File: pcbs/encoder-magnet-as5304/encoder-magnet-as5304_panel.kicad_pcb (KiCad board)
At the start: 2 copper layers, 39 x 25 mm, 168 parts, among them J1 BM05B-GHS, Q1 BC807-40LWX, U1 AS5304

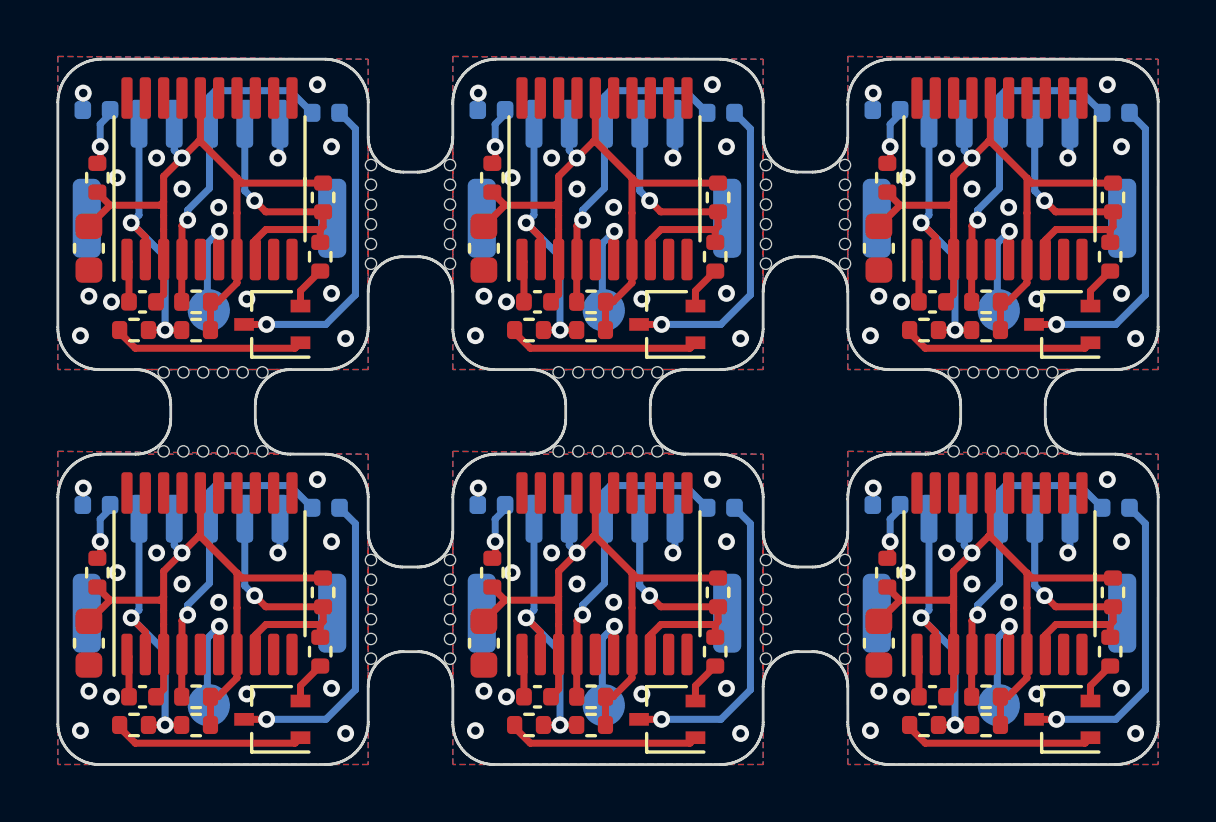
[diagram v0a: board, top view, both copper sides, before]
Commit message: Manually redraw broken outline for panelized AS5304 PCB
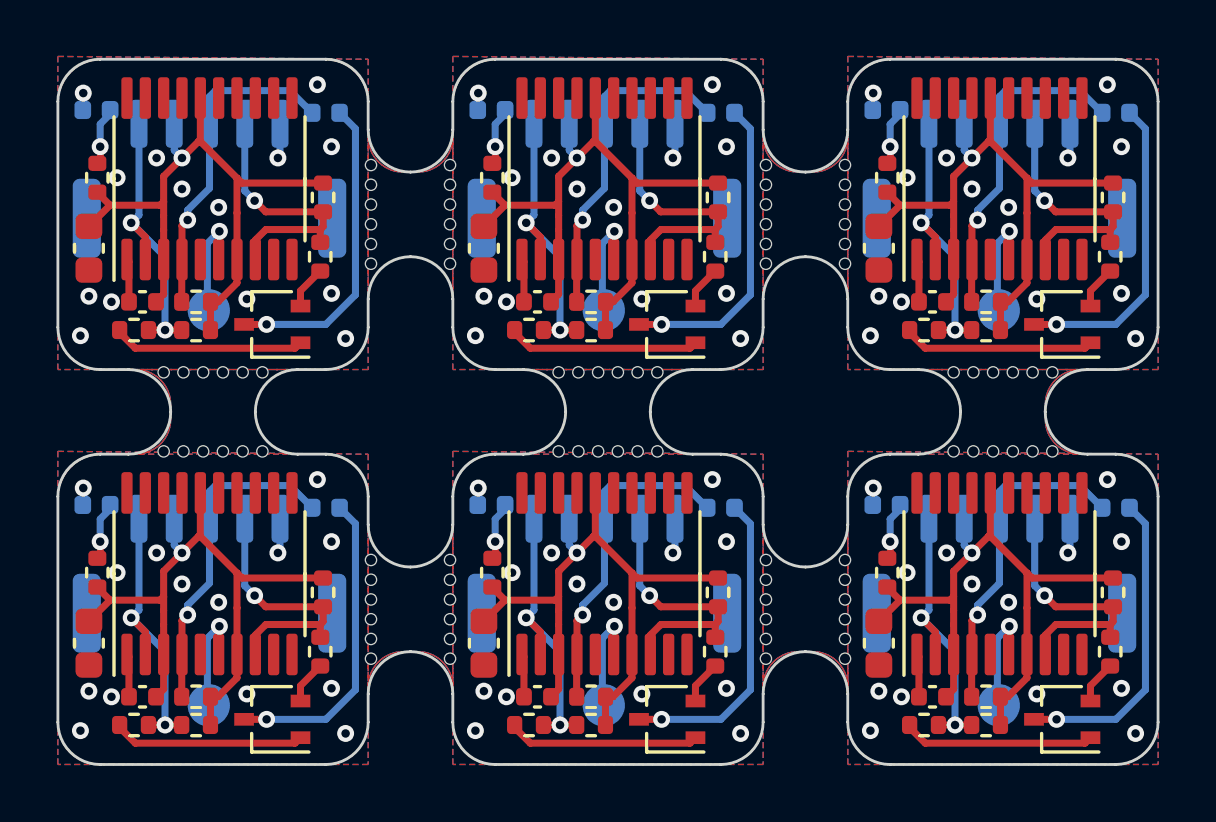
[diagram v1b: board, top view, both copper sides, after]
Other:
- outline, holes or cut-outs redrawn
